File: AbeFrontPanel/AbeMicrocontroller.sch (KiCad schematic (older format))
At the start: 17 parts

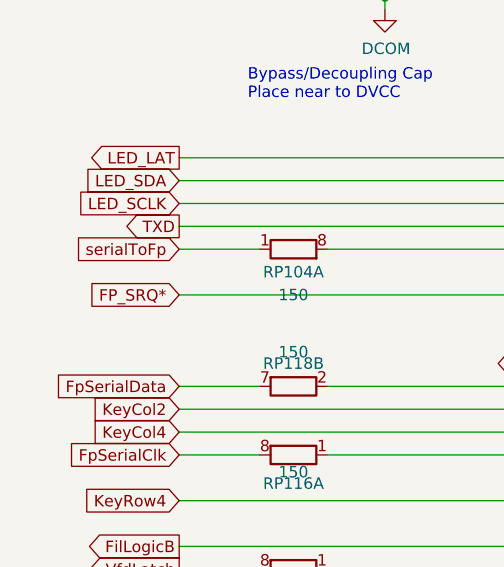
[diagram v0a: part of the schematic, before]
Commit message: Revise the value of TLV1117 R2/R1. Changed LED_SDA to LED_MOSI
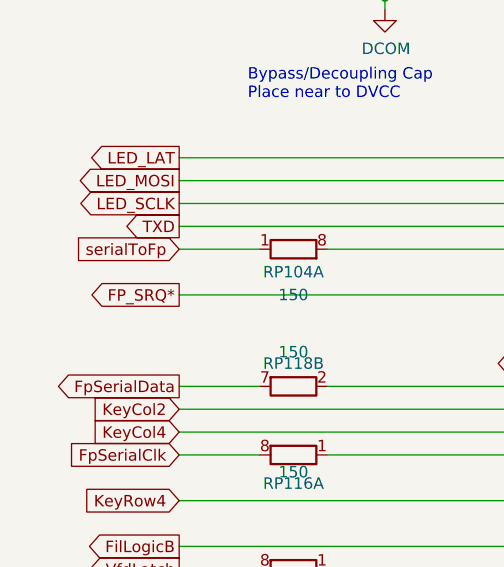
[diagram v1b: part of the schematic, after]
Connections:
- net LED_SDA: no longer U?.12 (P1-2_UCB0SIMO_UCB0SDA_TA0-2_A2_VEREF-)
- new net LED_MOSI: U?.12 (P1-2_UCB0SIMO_UCB0SDA_TA0-2_A2_VEREF-)
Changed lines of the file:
@@
 Wire Wire Line
 	9750 6200 9750 6250
-Text GLabel 1000 3750 0    50   Input ~ 0
+Text GLabel 1000 3750 0    50   Output ~ 0
 FP_SRQ*
 $Comp
@@
 	0    -1   -1   0
 $EndComp
-Text GLabel 1000 4150 0    50   Input ~ 0
+Text GLabel 1000 4150 0    50   Output ~ 0
 FpSerialData
 Wire Wire Line
@@
 Wire Wire Line
 	1000 4450 1350 4450
-Text GLabel 1000 3350 0    50   Input ~ 0
+Text GLabel 1000 3350 0    50   Output ~ 0
 LED_SCLK
-Text GLabel 1000 3250 0    50   Input ~ 0
-LED_SDA
+Text GLabel 1000 3250 0    50   Output ~ 0
+LED_MOSI
 Wire Wire Line
 	1000 3250 2850 3250
